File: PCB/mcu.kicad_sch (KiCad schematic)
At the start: 59 parts, among them J1 302-R161, J2 0731375003, J3 0731375003, SW2 PTS645VH58-2 LFS, SW3 TS04-66-50-BK-160-SMT, U24 RP2354B, U25 W25Q128JVS, Y1 ABM8AIG-12.000MHZ-12-2Z-T3

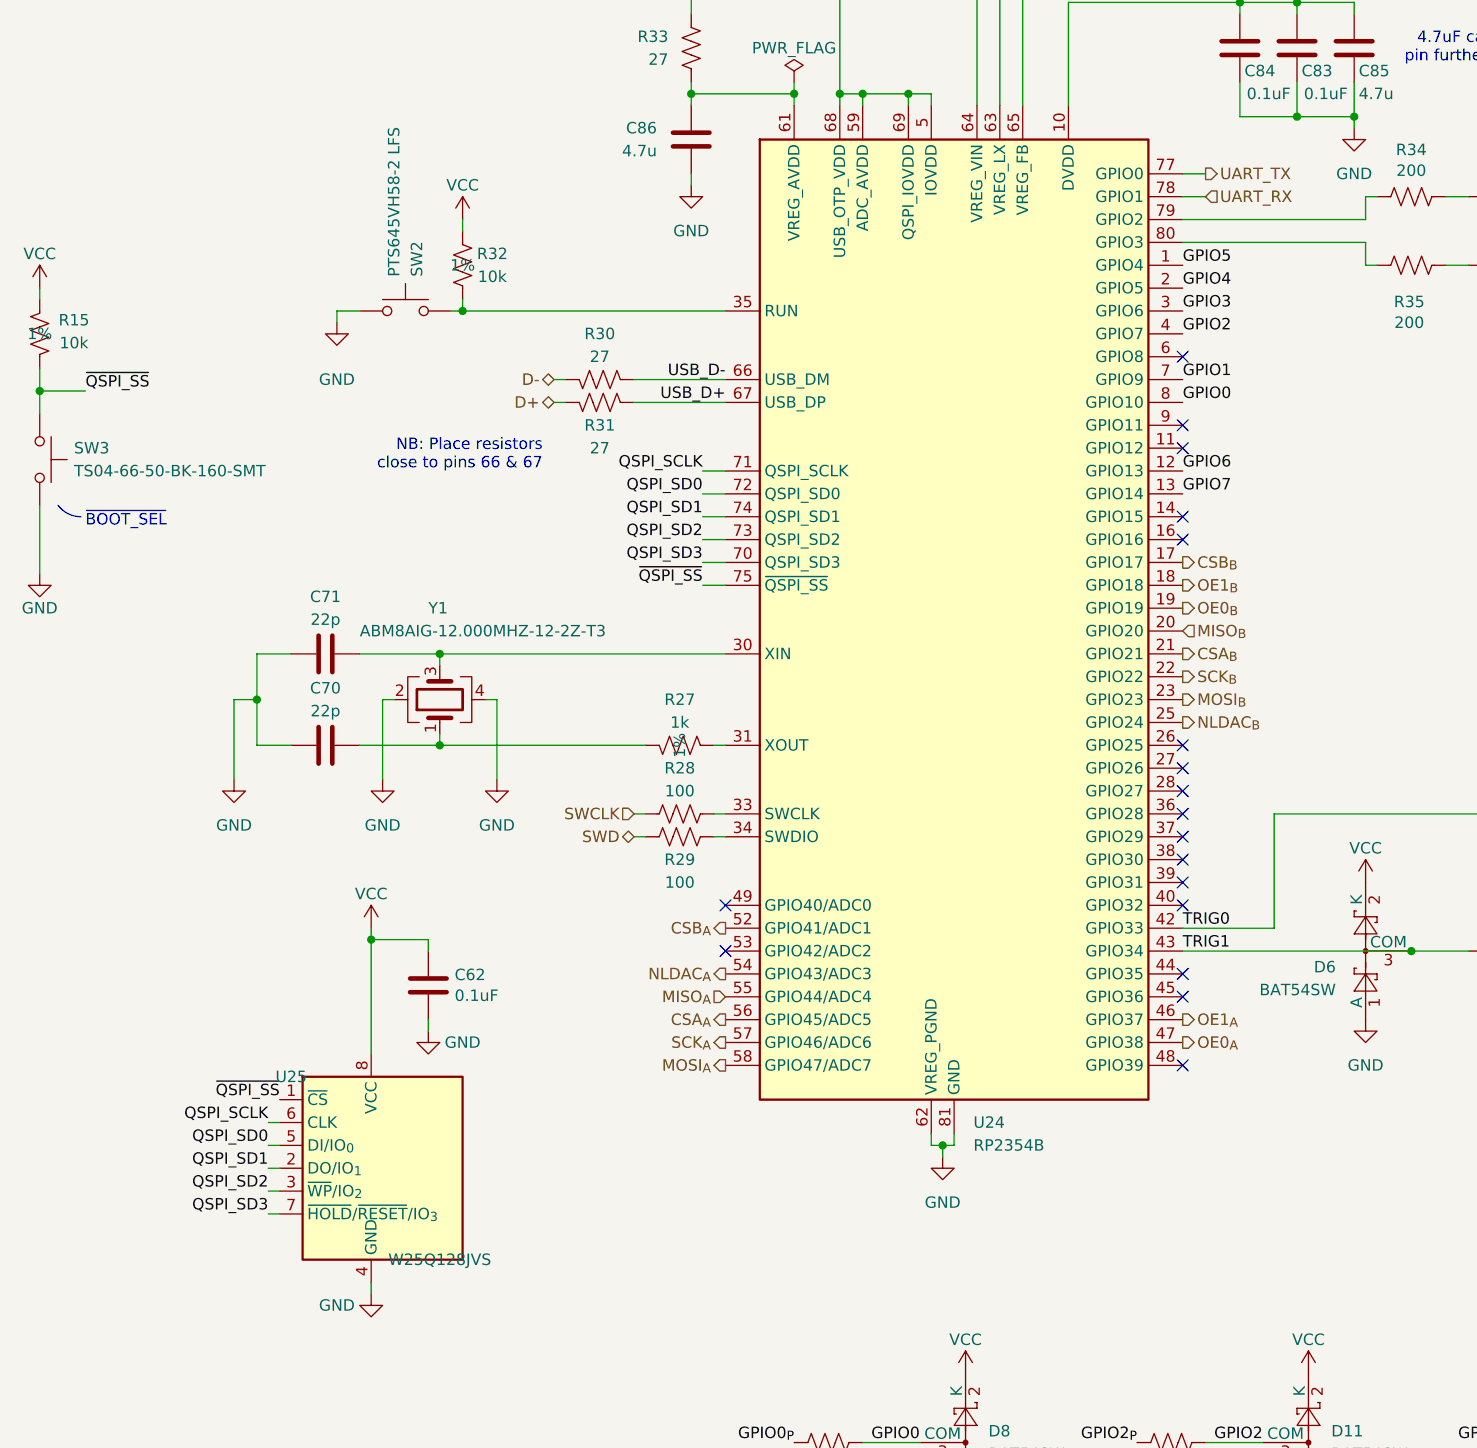
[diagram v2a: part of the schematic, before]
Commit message: Replace amplifiers
- INA826 -> AD8421
- AMP03 -> LT1995 w/ op-amp in feedback circuit
- Also:
  - update to kicad v10
  - utilize multi-channel layout feature
  - update calculations on schematic
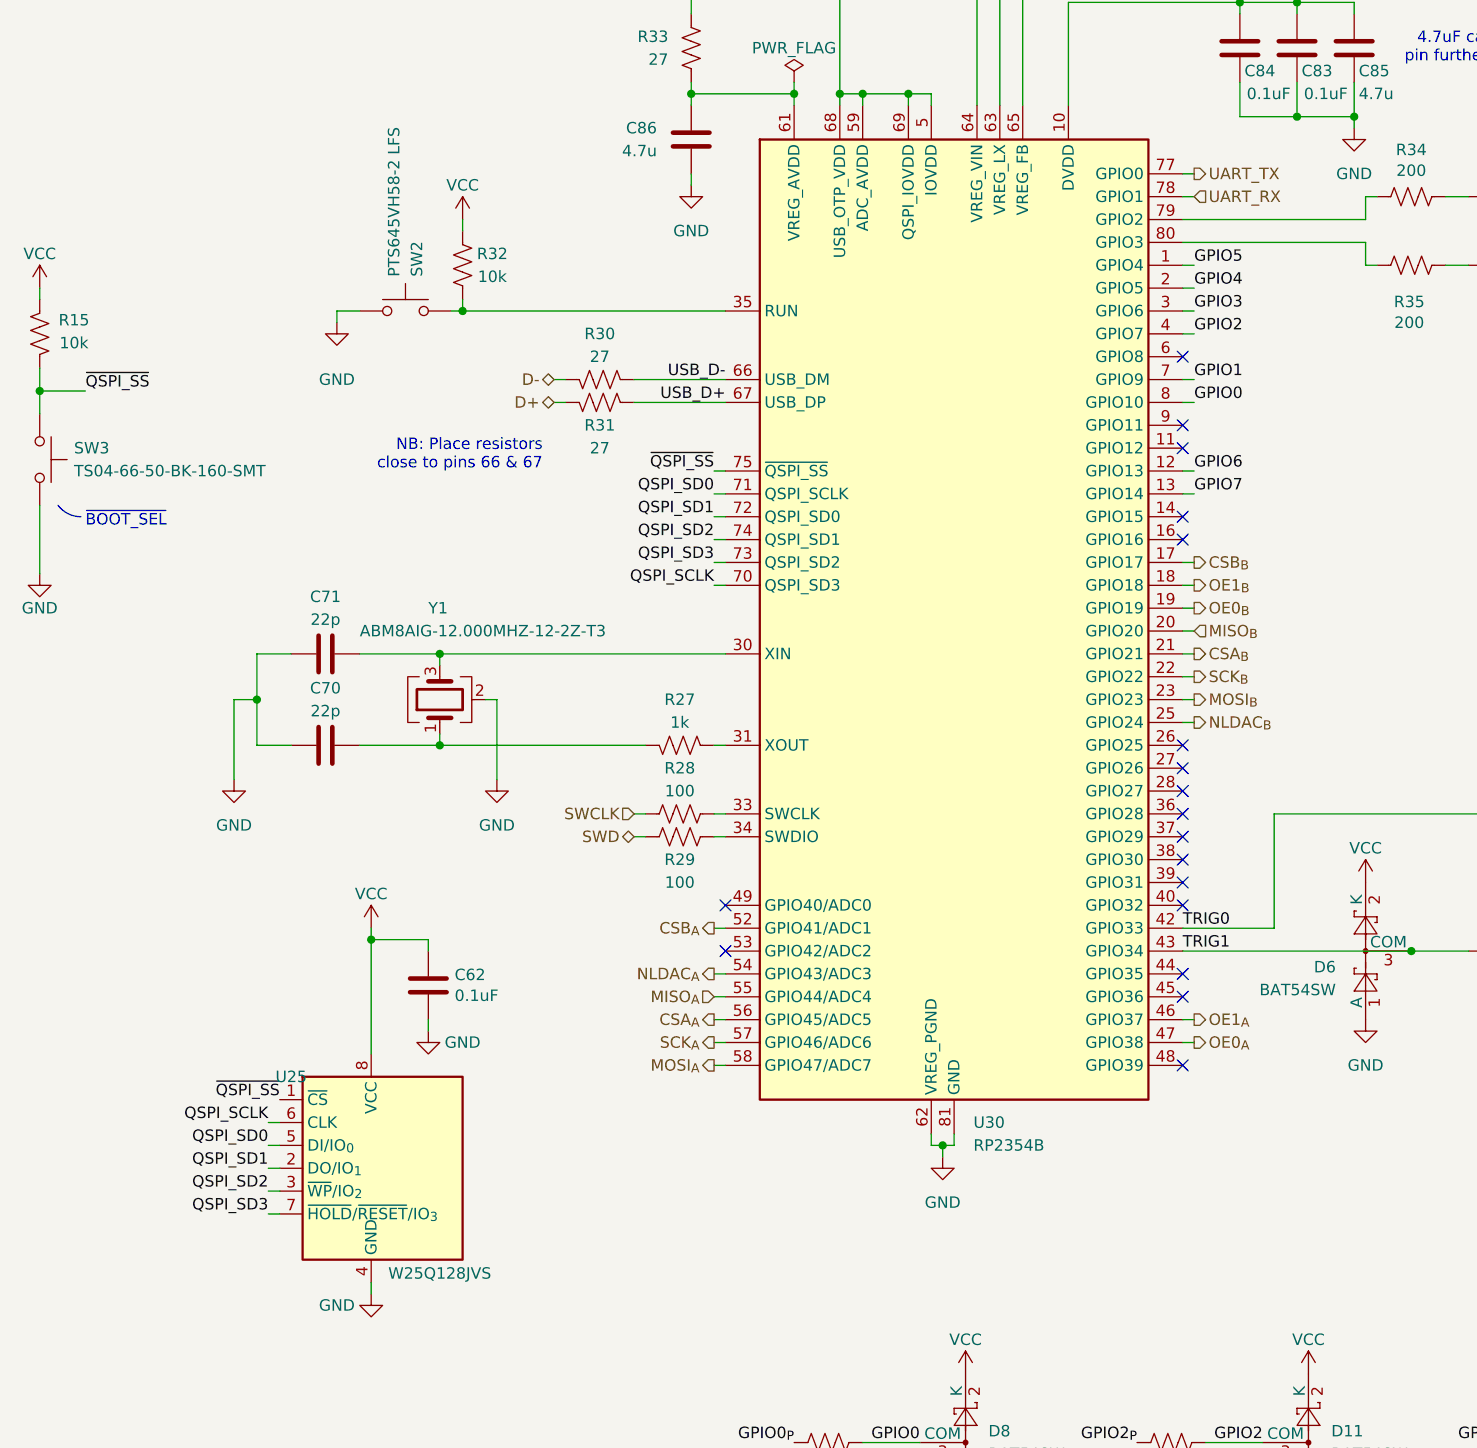
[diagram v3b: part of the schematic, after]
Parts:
- removed U24: RP2354B, Package_DFN_QFN:QFN-80-1EP_10x10mm_P0.4mm_EP3.4x3.4mm_ThermalVias, symbol open-ephys:RP2354B
- added U30: RP2354B, Package_DFN_QFN:QFN-80-1EP_10x10mm_P0.4mm_EP3.4x3.4mm, symbol MCU_RaspberryPi:RP2354B
- R15, R32: Tolerance 1% -> (none)
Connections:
- net +1V1: now also U30.10 (DVDD), U30.32 (DVDD), U30.51 (DVDD), U30.65 (VREG_FB)
- net CSA_{A}: now also U30.56 (GPIO45/ADC5)
- net CSA_{B}: now also U30.21 (GPIO21)
- net CSB_{A}: now also U30.52 (GPIO41/ADC1)
- net CSB_{B}: now also U30.17 (GPIO17)
- net GND: now also U30.62 (VREG_PGND), U30.81 (GND)
- net GPIO0: now also U30.8 (GPIO10)
- net GPIO1: now also U30.7 (GPIO9)
- net GPIO2: now also U30.4 (GPIO7)
- net GPIO3: now also U30.3 (GPIO6)
- net GPIO4: now also U30.2 (GPIO5)
- net GPIO5: now also U30.1 (GPIO4)
- net GPIO6: now also U30.12 (GPIO13)
- net GPIO7: now also U30.13 (GPIO14)
- net MISO_{A}: now also U30.55 (GPIO44/ADC4)
- net MISO_{B}: now also U30.20 (GPIO20)
- net MOSI_{A}: now also U30.58 (GPIO47/ADC7)
- net MOSI_{B}: now also U30.23 (GPIO23)
- net NLDAC_{A}: now also U30.54 (GPIO43/ADC3)
- net NLDAC_{B}: now also U30.25 (GPIO24)
- net OE0_{A}: now also U30.47 (GPIO38)
- net OE0_{B}: now also U30.19 (GPIO19)
- net OE1_{A}: now also U30.46 (GPIO37)
- net OE1_{B}: now also U30.18 (GPIO18)
- net QSPI_SCLK: now also U30.70 (QSPI_SD3)
- net QSPI_SD0: now also U30.71 (QSPI_SCLK)
- net QSPI_SD1: now also U30.72 (QSPI_SD0)
- net QSPI_SD2: now also U30.74 (QSPI_SD1)
- net QSPI_SD3: now also U30.73 (QSPI_SD2)
- net SCK_{A}: now also U30.57 (GPIO46/ADC6)
- net SCK_{B}: now also U30.22 (GPIO22)
- net TRIG0: now also U30.42 (GPIO33)
- net TRIG1: now also U30.43 (GPIO34)
- net UART_RX: now also U30.78 (GPIO1)
- net UART_TX: now also U30.77 (GPIO0)
- net USB_D+: now also U30.67 (USB_DP)
- net USB_D-: now also U30.66 (USB_DM)
- net VCC: now also U30.15 (IOVDD), U30.24 (IOVDD), U30.29 (IOVDD), U30.41 (IOVDD), U30.5 (IOVDD), U30.50 (IOVDD), U30.59 (ADC_AVDD), U30.60 (IOVDD), U30.64 (VREG_VIN), U30.68 (USB_OTP_VDD), U30.69 (QSPI_IOVDD), U30.76 (IOVDD)
- net ~{QSPI_SS}: now also U30.75 (~{QSPI_SS})
- net at R32.2, SW2.2: now also U30.35 (RUN)
- net at C86.1, R33.2: now also U30.61 (VREG_AVDD)
- net at R28.2: now also U30.33 (SWCLK)
- net at L1.2: now also U30.63 (VREG_LX)
- net at R35.2: now also U30.80 (GPIO3)
- net at R27.1: now also U30.31 (XOUT)
- net at C71.2, Y1.3: now also U30.30 (XIN)
- net at R29.2: now also U30.34 (SWDIO)
- net at R34.2: now also U30.79 (GPIO2)
